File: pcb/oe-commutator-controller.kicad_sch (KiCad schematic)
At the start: 9 parts

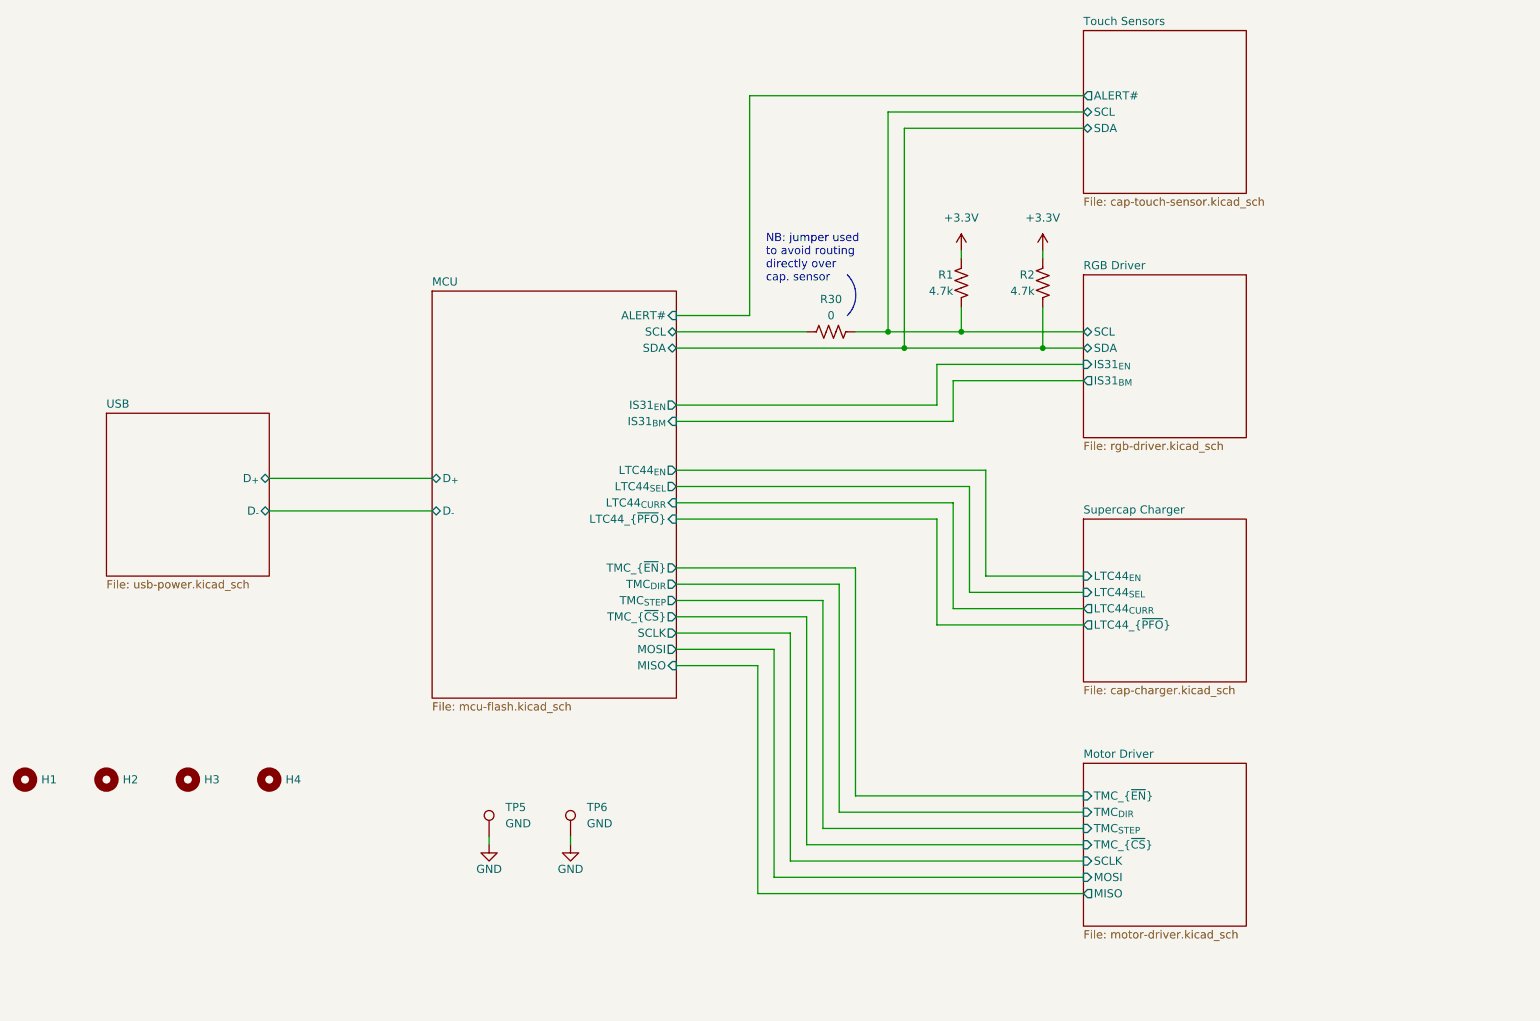
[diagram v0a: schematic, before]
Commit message: Final edits to rev G before fab
- Move USB connector twoards board edge by 1.5mm
- Make all silk text uniform
- Add required stackup and board characteristics to user.comments layer
- Redo 3.3V power routing to RP2040 (one power pin was not connected)
- Uniform schematic sheet size
- And many other small changes
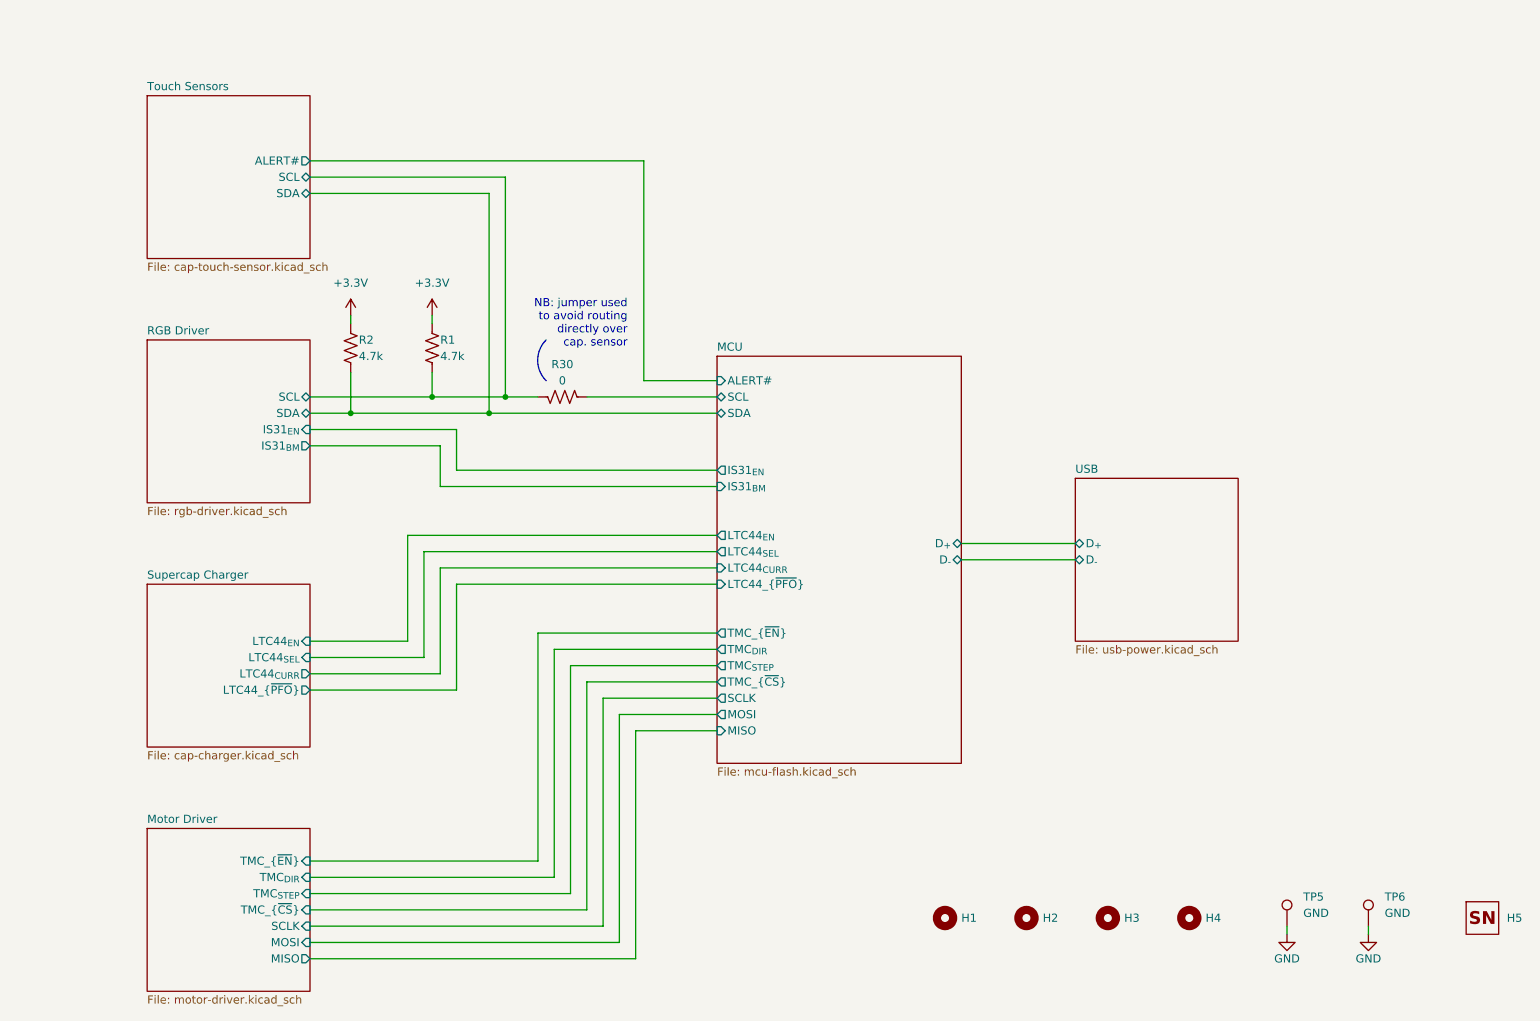
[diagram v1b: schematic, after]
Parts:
- added H5: ~, open-ephys:OEPS_SN-STICKER-5x5mm, symbol open-ephys:OEPS-SN
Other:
- moved on the sheet: H1, H2, H3, H4, R1, R2, R30, TP5, TP6

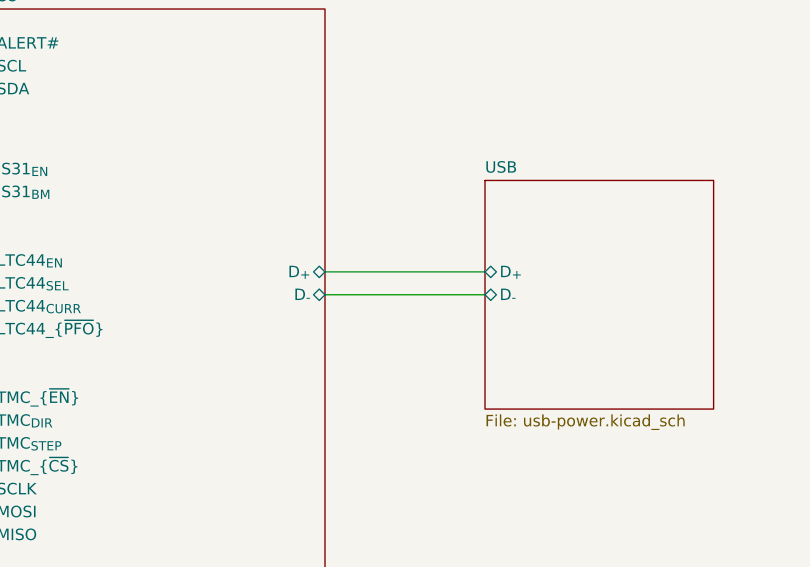
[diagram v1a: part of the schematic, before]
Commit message: Add USB diode protection
- Change revision g -> h
  - schematic
  - pcb
  - silk screen
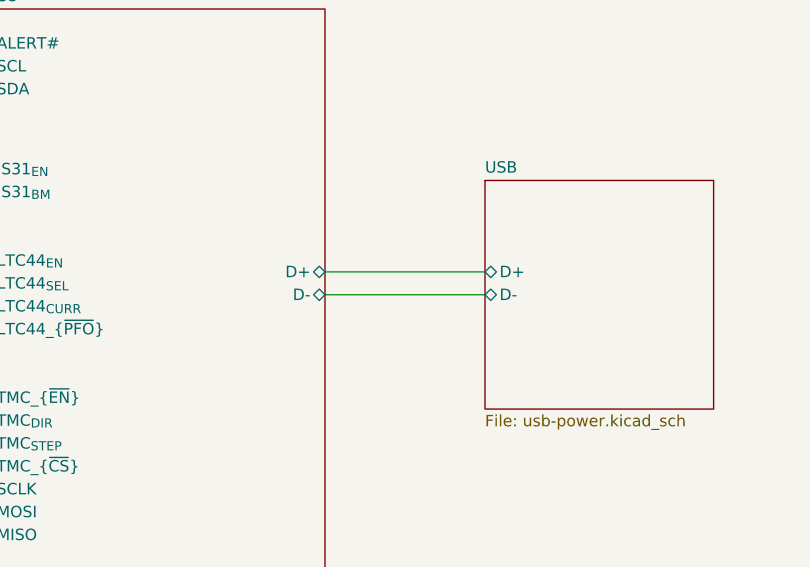
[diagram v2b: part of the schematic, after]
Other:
- sheet MCU ports: added D+, D-; removed D_{+}, D_{-}
- sheet USB ports: added D+, D-; removed D_{+}, D_{-}
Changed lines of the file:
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@@
 (kicad_sch
-	(version 20241209)
+	(version 20250114)
 	(generator "eeschema")
 	(generator_version "9.0")
@@
 	(title_block
 		(title "Open Ephys Commutator Controller")
-		(rev "G")
+		(rev "H")
 		(company "Open Ephys, Inc.")
 		(comment 1 "Cris Sharp")
@@
 			)
 		)
-		(pin "D_{-}" bidirectional
+		(pin "D-" bidirectional
 			(at 201.93 101.6 180)
 			(effects
@@
 			)
 		)
-		(pin "D_{+}" bidirectional
+		(pin "D+" bidirectional
 			(at 201.93 99.06 180)
 			(effects
@@
 			)
 		)
-		(pin "D_{-}" bidirectional
+		(pin "D-" bidirectional
 			(at 184.15 101.6 0)
 			(effects
@@
 			)
 		)
-		(pin "D_{+}" bidirectional
+		(pin "D+" bidirectional
 			(at 184.15 99.06 0)
 			(effects

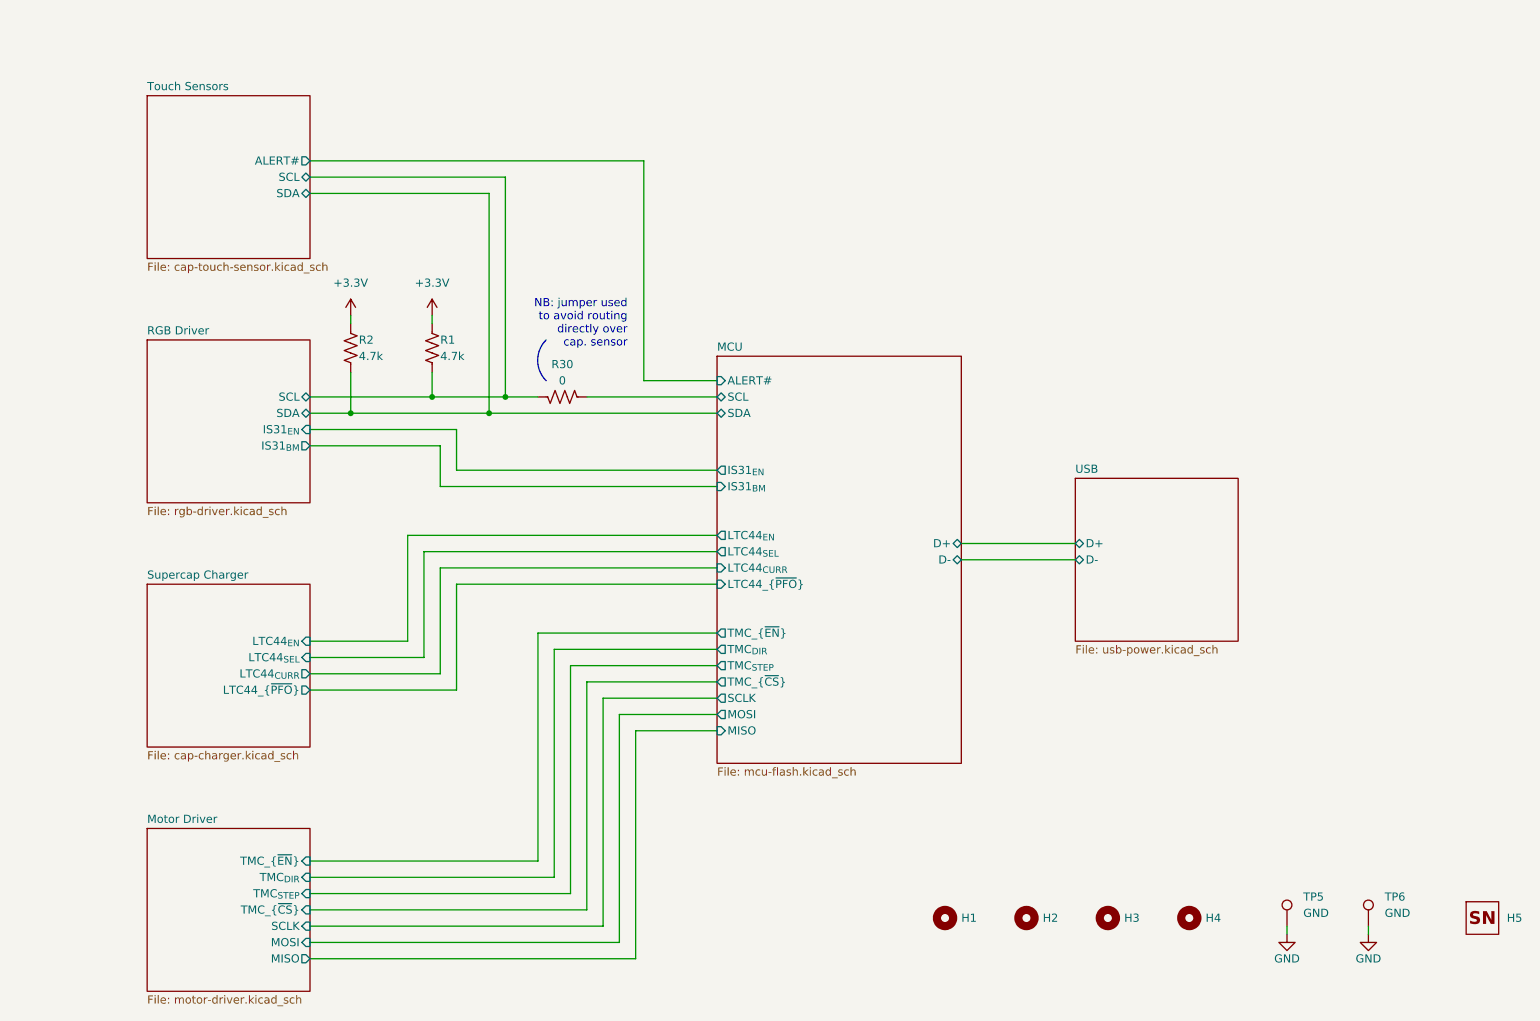
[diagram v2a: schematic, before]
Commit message: Lower sense resistance (0.5 -> 0.43 Ohms)
Also:
- Route TMC2130 diagnostic pins to RP2040
- Instead of manually excluding violations:
  - Changed spoke minimum: 2 -> 1
  - Changed copper-to-hole clearance: 0.25mm -> 0.19mm
- Update revision labels on sch, pcb, and silkscreen
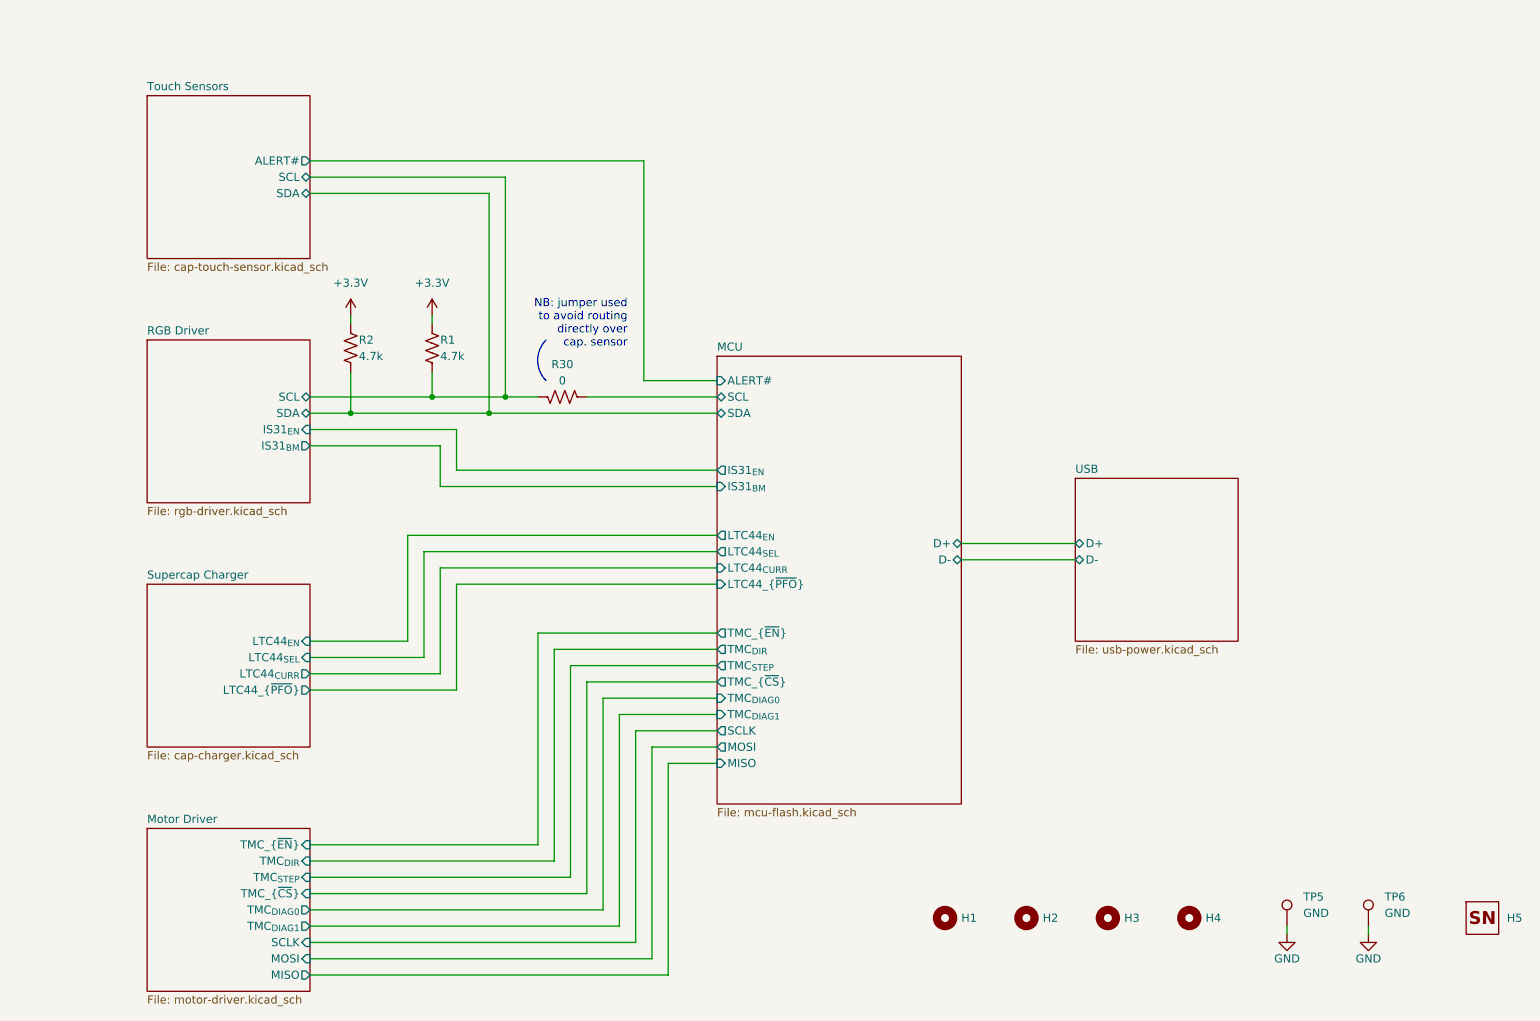
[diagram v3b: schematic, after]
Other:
- sheet MCU ports: added TMC_{DIAG0}, TMC_{DIAG1}; removed none
- sheet Motor Driver ports: added TMC_{DIAG0}, TMC_{DIAG1}; removed none
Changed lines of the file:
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@@
 	(title_block
 		(title "Open Ephys Commutator Controller")
-		(rev "H")
+		(rev "I")
 		(company "Open Ephys, Inc.")
 		(comment 1 "Cris Sharp")
@@
 	(wire
 		(pts
-			(xy 118.11 113.03) (xy 118.11 148.59)
+			(xy 118.11 113.03) (xy 118.11 146.05)
 		)
 		(stroke
@@
 	(wire
 		(pts
-			(xy 130.81 125.73) (xy 130.81 161.29)
-		)
-		(stroke
-			(width 0)
-			(type default)
-		)
-	)
-	(wire
-		(pts
-			(xy 146.05 123.19) (xy 128.27 123.19)
+			(xy 135.89 130.81) (xy 135.89 163.83)
+		)
+		(stroke
+			(width 0)
+			(type default)
+		)
+	)
+	(wire
+		(pts
+			(xy 146.05 128.27) (xy 133.35 128.27)
+		)
+		(stroke
+			(width 0)
+			(type default)
+		)
+	)
+	(wire
+		(pts
+			(xy 128.27 123.19) (xy 146.05 123.19)
 		)
 		(stroke
@@
 	(wire
 		(pts
-			(xy 118.11 148.59) (xy 82.55 148.59)
+			(xy 118.11 146.05) (xy 82.55 146.05)
 		)
 		(stroke
@@
 	(wire
 		(pts
-			(xy 128.27 158.75) (xy 82.55 158.75)
+			(xy 133.35 161.29) (xy 82.55 161.29)
 		)
 		(stroke
@@
 	(wire
 		(pts
-			(xy 146.05 128.27) (xy 133.35 128.27)
+			(xy 82.55 156.21) (xy 128.27 156.21)
+		)
+		(stroke
+			(width 0)
+			(type default)
+		)
+	)
+	(wire
+		(pts
+			(xy 146.05 133.35) (xy 138.43 133.35)
 		)
 		(stroke
@@
 	(wire
 		(pts
+			(xy 128.27 156.21) (xy 128.27 123.19)
+		)
+		(stroke
+			(width 0)
+			(type default)
+		)
+	)
+	(wire
+		(pts
 			(xy 88.9 63.5) (xy 88.9 64.77)
 		)
@@
 	(wire
 		(pts
-			(xy 128.27 123.19) (xy 128.27 158.75)
-		)
-		(stroke
-			(width 0)
-			(type default)
-		)
-	)
-	(wire
-		(pts
-			(xy 133.35 128.27) (xy 133.35 163.83)
+			(xy 133.35 128.27) (xy 133.35 161.29)
+		)
+		(stroke
+			(width 0)
+			(type default)
+		)
+	)
+	(wire
+		(pts
+			(xy 138.43 133.35) (xy 138.43 166.37)
 		)
 		(stroke
@@
 	(wire
 		(pts
-			(xy 133.35 163.83) (xy 82.55 163.83)
-		)
-		(stroke
-			(width 0)
-			(type default)
-		)
-	)
-	(wire
-		(pts
-			(xy 123.19 153.67) (xy 82.55 153.67)
+			(xy 138.43 166.37) (xy 82.55 166.37)
+		)
+		(stroke
+			(width 0)
+			(type default)
+		)
+	)
+	(wire
+		(pts
+			(xy 123.19 151.13) (xy 82.55 151.13)
 		)
 		(stroke
@@
 	(wire
 		(pts
+			(xy 130.81 125.73) (xy 146.05 125.73)
+		)
+		(stroke
+			(width 0)
+			(type default)
+		)
+	)
+	(wire
+		(pts
 			(xy 105.41 121.92) (xy 82.55 121.92)
 		)
@@
 	(wire
 		(pts
-			(xy 146.05 125.73) (xy 130.81 125.73)
+			(xy 146.05 130.81) (xy 135.89 130.81)
 		)
 		(stroke
@@
 	(wire
 		(pts
-			(xy 123.19 118.11) (xy 123.19 153.67)
+			(xy 123.19 118.11) (xy 123.19 151.13)
 		)
 		(stroke
@@
 	(wire
 		(pts
-			(xy 125.73 120.65) (xy 125.73 156.21)
+			(xy 125.73 120.65) (xy 125.73 153.67)
 		)
 		(stroke
@@
 	(wire
 		(pts
+			(xy 130.81 158.75) (xy 130.81 125.73)
+		)
+		(stroke
+			(width 0)
+			(type default)
+		)
+	)
+	(wire
+		(pts
 			(xy 146.05 76.2) (xy 125.73 76.2)
 		)
@@
 	(wire
 		(pts
-			(xy 120.65 115.57) (xy 120.65 151.13)
+			(xy 120.65 115.57) (xy 120.65 148.59)
 		)
 		(stroke
@@
 	(wire
 		(pts
-			(xy 120.65 151.13) (xy 82.55 151.13)
+			(xy 120.65 148.59) (xy 82.55 148.59)
 		)
 		(stroke
@@
 	(wire
 		(pts
-			(xy 125.73 156.21) (xy 82.55 156.21)
+			(xy 125.73 153.67) (xy 82.55 153.67)
 		)
 		(stroke
@@
 	(wire
 		(pts
-			(xy 130.81 161.29) (xy 82.55 161.29)
+			(xy 135.89 163.83) (xy 82.55 163.83)
 		)
 		(stroke
@@
 		(pts
 			(xy 88.9 72.39) (xy 88.9 78.74)
+		)
+		(stroke
+			(width 0)
+			(type default)
+		)
+	)
+	(wire
+		(pts
+			(xy 82.55 158.75) (xy 130.81 158.75)
 		)
 		(stroke
@@
 		)
 		(pin "TMC_{~{EN}}" input
+			(at 82.55 146.05 0)
+			(effects
+				(font
+					(size 1.27 1.27)
+				)
+				(justify right)
+			)
+		)
+		(pin "MISO" output
+			(at 82.55 166.37 0)
+			(effects
+				(font
+					(size 1.27 1.27)
+				)
+				(justify right)
+			)
+		)
+		(pin "MOSI" input
+			(at 82.55 163.83 0)
+			(effects
+				(font
+					(size 1.27 1.27)
+				)
+				(justify right)
+			)
+		)
+		(pin "TMC_{~{CS}}" input
+			(at 82.55 153.67 0)
+			(effects
+				(font
+					(size 1.27 1.27)
+				)
+				(justify right)
+			)
+		)
+		(pin "SCLK" input
+			(at 82.55 161.29 0)
+			(effects
+				(font
+					(size 1.27 1.27)
+				)
+				(justify right)
+			)
+		)
+		(pin "TMC_{DIR}" input
 			(at 82.55 148.59 0)
 			(effects
@@
 			)
 		)
-		(pin "MISO" output
-			(at 82.55 163.83 0)
+		(pin "TMC_{STEP}" input
+			(at 82.55 151.13 0)
 			(effects
 				(font
@@
 			)
 		)
-		(pin "MOSI" input
-			(at 82.55 161.29 0)
+		(pin "TMC_{DIAG0}" output
+			(at 82.55 156.21 0)
 			(effects
 				(font
@@
 			)
 		)
-		(pin "TMC_{~{CS}}" input
-			(at 82.55 156.21 0)
-			(effects
-				(font
-					(size 1.27 1.27)
-				)
-				(justify right)
-			)
-		)
-		(pin "SCLK" input
+		(pin "TMC_{DIAG1}" output
 			(at 82.55 158.75 0)
-			(effects
-				(font
-					(size 1.27 1.27)
-				)
-				(justify right)
-			)
-		)
-		(pin "TMC_{DIR}" input
-			(at 82.55 151.13 0)
-			(effects
-				(font
-					(size 1.27 1.27)
-				)
-				(justify right)
-			)
-		)
-		(pin "TMC_{STEP}" input
-			(at 82.55 153.67 0)
 			(effects
 				(font
@@
 	(sheet
 		(at 146.05 69.85)
-		(size 38.1 63.5)
+		(size 38.1 69.85)
 		(exclude_from_sim no)
 		(in_bom yes)
@@
 		)
 		(property "Sheetfile" "mcu-flash.kicad_sch"
-			(at 146.05 133.9346 0)
+			(at 146.05 140.2846 0)
 			(effects
 				(font
@@
 		)
 		(pin "MISO" input
-			(at 146.05 128.27 180)
+			(at 146.05 133.35 180)
 			(effects
 				(font
@@
 		)
 		(pin "SCLK" output
-			(at 146.05 123.19 180)
+			(at 146.05 128.27 180)
 			(effects
 				(font
@@
 		)
 		(pin "MOSI" output
-			(at 146.05 125.73 180)
+			(at 146.05 130.81 180)
 			(effects
 				(font
@@
 			(effects
 				(font
+					(size 1.27 1.27)
+				)
+				(justify left)
+			)
+		)
+		(pin "TMC_{DIAG0}" input
+			(at 146.05 123.19 180)
+			(effects
+				(font
+					(size 1.27 1.27)
+				)
+				(justify left)
+			)
+		)
+		(pin "TMC_{DIAG1}" input
+			(at 146.05 125.73 180)
+			(effects
+				(font
